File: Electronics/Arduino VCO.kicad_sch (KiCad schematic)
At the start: 45 parts, among them U1 TL072

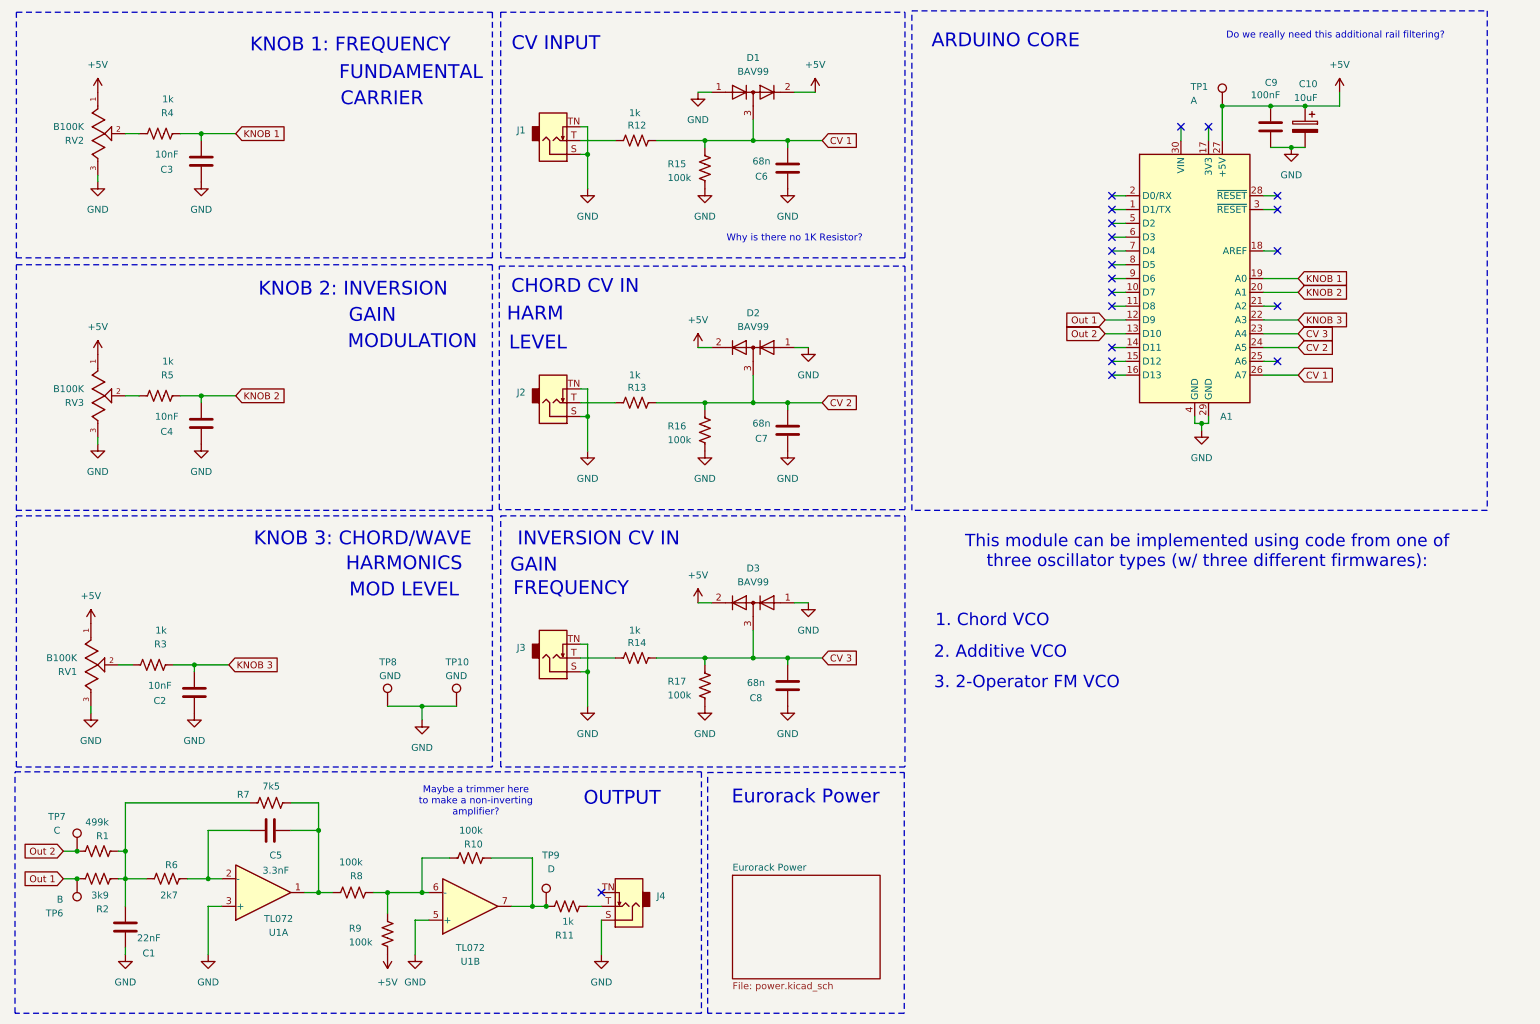
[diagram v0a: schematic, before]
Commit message: Fix formatting in README.md and add VCO schematic files
- Updated mathematical notation in README.md to use \mathrm{} for consistency.
- Added new KiCad project file for VCO schematic (vco.kicad_prl).
- Created a lock file for the KiCad project to track user session information.
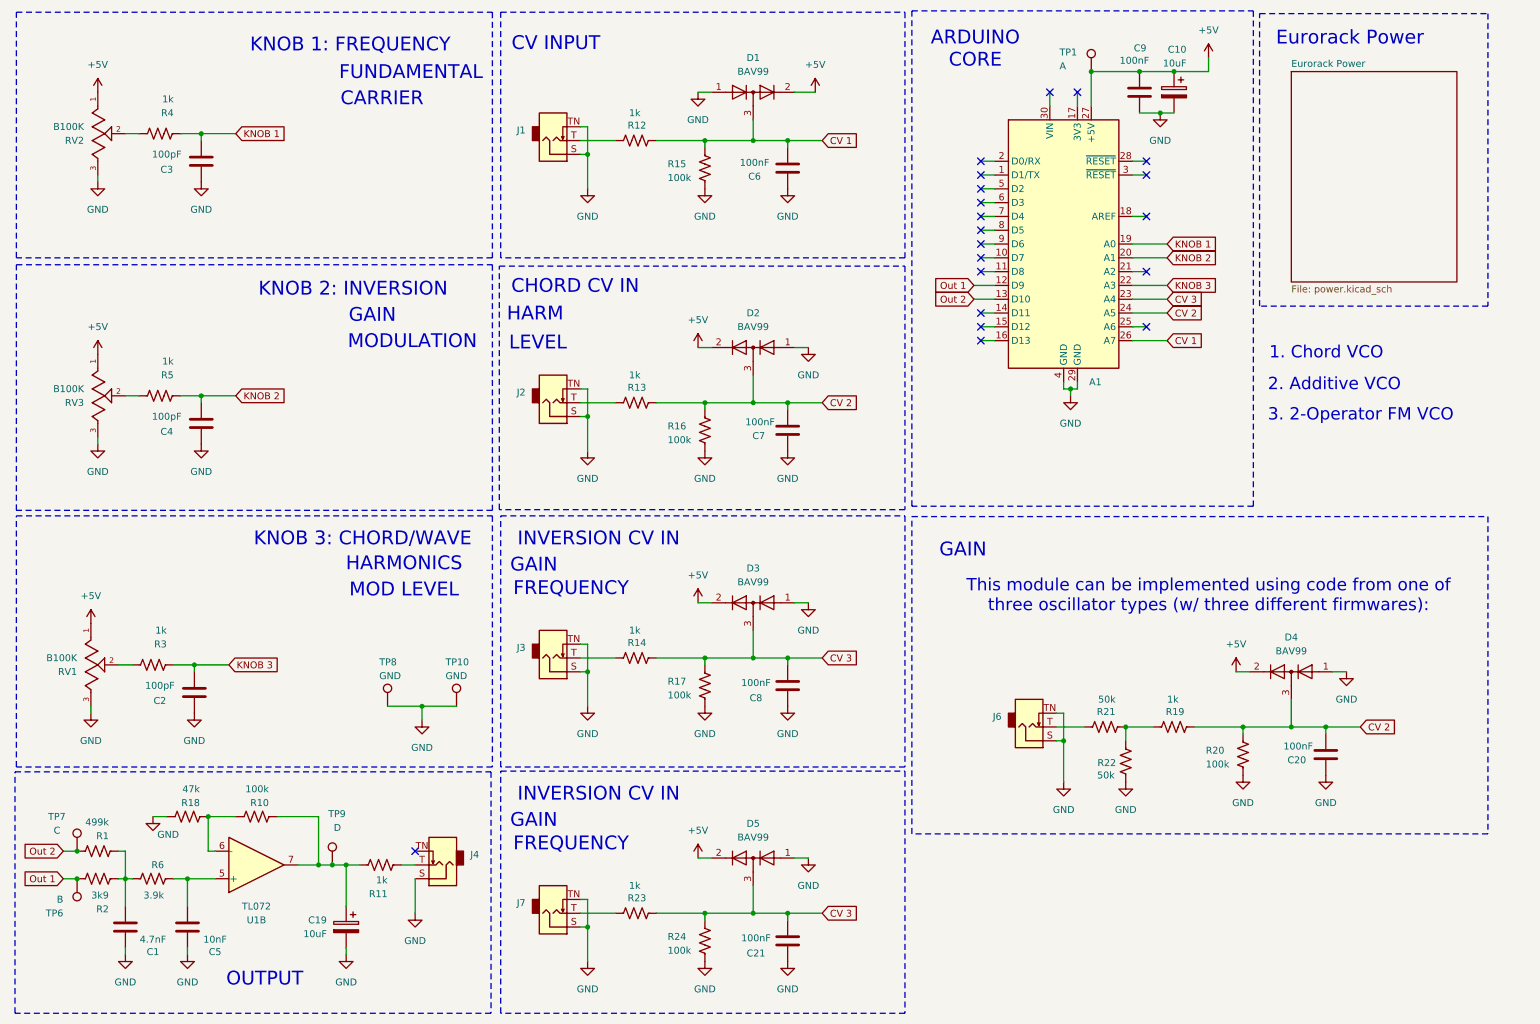
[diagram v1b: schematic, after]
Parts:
- removed R7: 7k5, Resistor_SMD:R_0805_2012Metric_Pad1.20x1.40mm_HandSolder, symbol Device:R_US
- removed R8, R9: 100k, Resistor_SMD:R_0805_2012Metric_Pad1.20x1.40mm_HandSolder, symbol Device:R_US
- removed unit 1 of U1
- added C19: 10uF, Capacitor_SMD:CP_Elec_5x5.4, symbol Device:C_Polarized
- added C20, C21: 100nF, Capacitor_SMD:C_0805_2012Metric_Pad1.18x1.45mm_HandSolder, symbol Device:C
- added D4, D5: BAV99, Package_TO_SOT_SMD:SOT-23, symbol Diode:BAV99
- added J6, J7: (no value), Eurorack:Jack_3.5mm_QingPu_WQP-PJ398SM_Vertical, symbol Connector_Audio:AudioJack2_SwitchT
- added R18: 47k, Resistor_SMD:R_0805_2012Metric_Pad1.20x1.40mm_HandSolder, symbol Device:R_US
- added R19, R23: 1k, Resistor_SMD:R_0805_2012Metric_Pad1.20x1.40mm_HandSolder, symbol Device:R_US
- added R20, R24: 100k, Resistor_SMD:R_0805_2012Metric_Pad1.20x1.40mm_HandSolder, symbol Device:R_US
- added R21, R22: 50k, Resistor_SMD:R_0805_2012Metric_Pad1.20x1.40mm_HandSolder, symbol Device:R_US
- C1: value 22nF -> 4.7nF
- C2, C3, C4: value 10nF -> 100pF
- C5: value 3.3nF -> 10nF
- C6, C7, C8: value 68n -> 100nF
- R6: value 2k7 -> 3.9k
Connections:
- net +5V: now also D4.2 (A), D5.2 (A)
- net CV 2: now also C20.2, D4.3 (K), R19.2, R20.2
- net CV 3: now also C21.2, D5.3 (K), R23.2, R24.2
- net GND: now also C5.2, C19.2, C20.1, C21.1, D4.1 (K), D5.1 (K), J6.S, J6.TN, J7.S, J7.TN, R18.1, R20.1, R22.1, R24.1; no longer U1.5 (+)
- net at C5.1: now also R6.2, U1.5 (+)
- net at R10.1, U1.6 (-): now also R18.2
- net at R10.2, R11.1, TP9.1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: now also C19.1
- new net: R19.1, R21.2, R22.2
- new net: J7.T, R23.1
- new net: J6.T, R21.1
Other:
- note removed: "Do we really need this additional rail filtering?"
- note removed: "Maybe a trimmer here to make a non-inverting amplifier?"
- note removed: "Why is there no 1K Resistor?"
- moved on the sheet: A1, C10, C9, J4, R10, R11, R6, TP1, TP9, U1B

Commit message: Add font configuration file for KiCad CLI reports
This commit introduces a new `fonts.conf` file to specify font directories and cache location for the KiCad CLI reports. The configuration includes standard system font directories as well as a user-specific font directory.
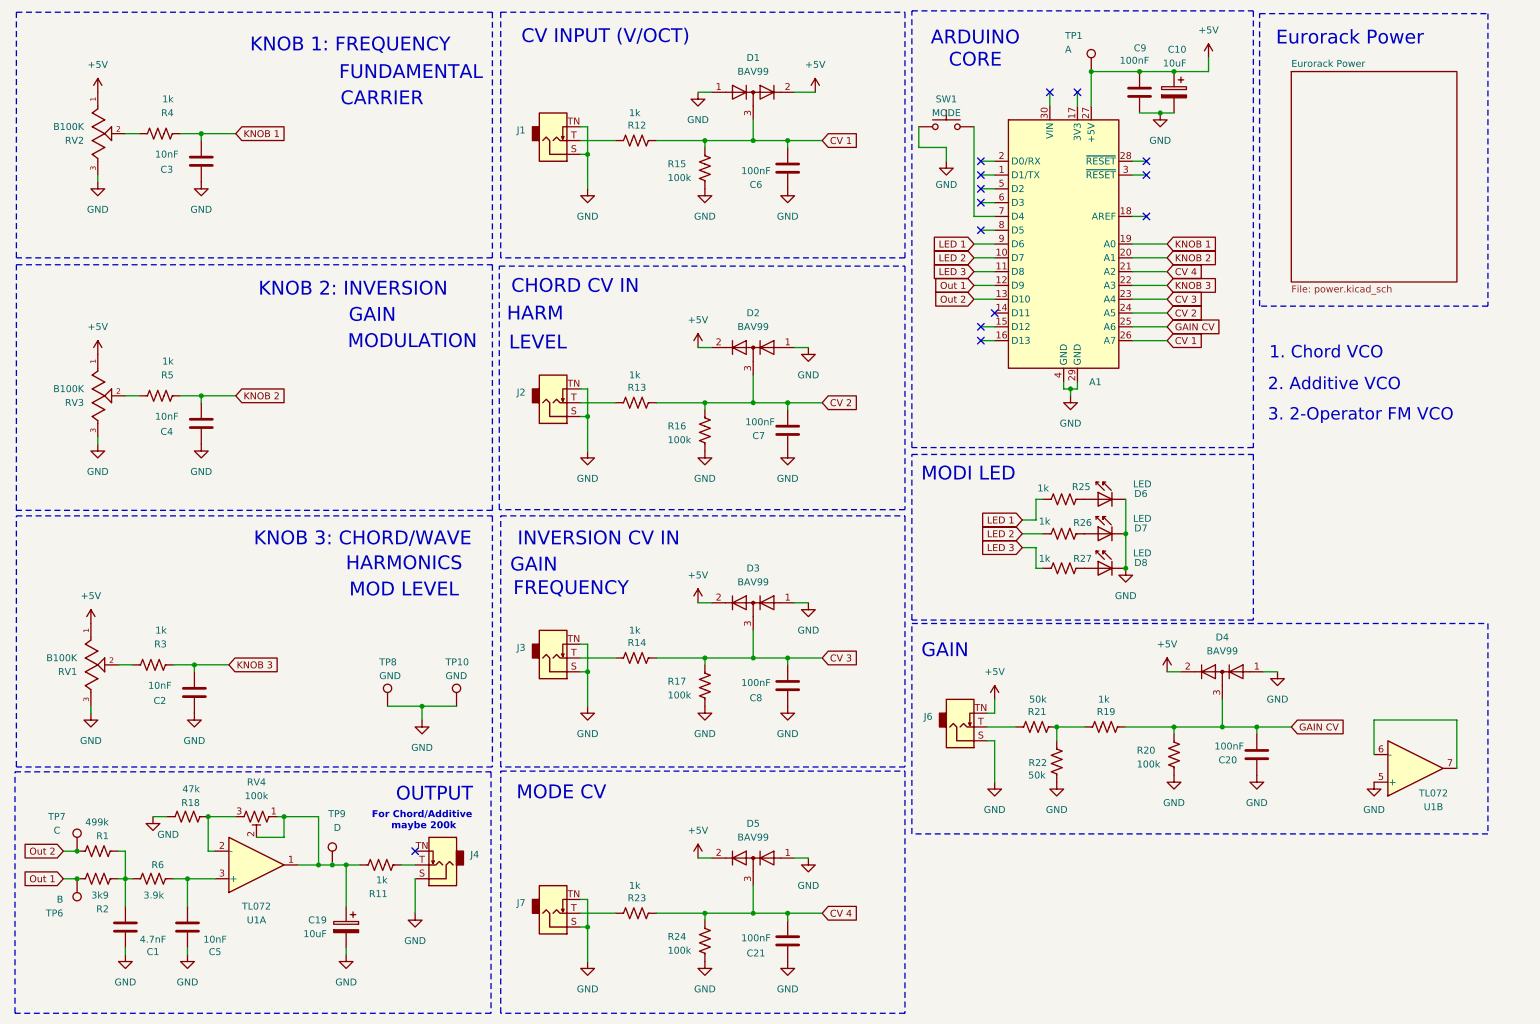
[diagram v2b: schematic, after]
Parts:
- removed R10: 100k, Resistor_SMD:R_0805_2012Metric_Pad1.20x1.40mm_HandSolder, symbol Device:R_US
- added D6, D7, D8: LED, LED_THT:LED_D3.0mm_IRBlack, symbol LED:IR204A
- added R25, R26, R27: 1k, Resistor_SMD:R_0805_2012Metric_Pad1.20x1.40mm_HandSolder, symbol Device:R_US
- added RV4: 100k, Eurorack:Trimmer_Bourns_3296W_50k_THT, symbol Device:R_Potentiometer_Trim_US
- added SW1: MODE, Button_Switch_THT:SW_PUSH_6mm, symbol Switch:SW_Push
- added unit 1 of U1
- C2, C3, C4: value 100pF -> 10nF
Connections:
- net +5V: now also J6.TN
- net CV 2: no longer C20.2, D4.3 (K), R19.2, R20.2
- net CV 3: no longer C21.2, D5.3 (K), R23.2, R24.2
- net GND: now also U1.5 (+), D6.1 (K), D7.1 (K), D8.1 (K), SW1.1; no longer J6.TN
- net at C5.1, R6.2: now also U1.3 (+); no longer U1.5 (+)
- net at R18.2: now also RV4.3, U1.2 (-); no longer U1.6 (-)
- net at C19.1, R11.1, TP9.1: now also RV4.1, RV4.2, U1.1; no longer U1.7
- net LED 2: now reaches A1.10 (D7)
- net LED 2: now also R26.1
- net LED 3: now reaches A1.11 (D8)
- net LED 3: now also R27.1
- net CV 4: now reaches A1.21 (A2)
- net CV 4: now also C21.2, D5.3 (K), R23.2, R24.2
- net GAIN CV: now reaches A1.25 (A6)
- net GAIN CV: now also C20.2, D4.3 (K), R19.2, R20.2
- net at A1.7 (D4): now also SW1.2
- net LED 1: now reaches A1.9 (D6)
- net LED 1: now also R25.1
- new net: D6.2 (A), R25.2
- new net: D8.2 (A), R27.2
- new net: D7.2 (A), R26.2
- new net: U1.6 (-), U1.7
- no-connect marks 20 -> 14
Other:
- note added: "CV INPUT (V/OCT)"
- note added: "For Chord/Additive maybe 200k"
- note added: "MODE CV"
- note added: "MODI LED"
- note removed: "CV INPUT"
- note removed: "This module can be implemented using code from one of three oscillator types (w/ three different firmwares):"
- moved on the sheet: C20, D4, J6, R19, R20, R21, R22
